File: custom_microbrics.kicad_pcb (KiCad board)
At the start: 2 copper layers, 20.2 x 20.2 mm, 2 parts, among them J1 Conn_01x03

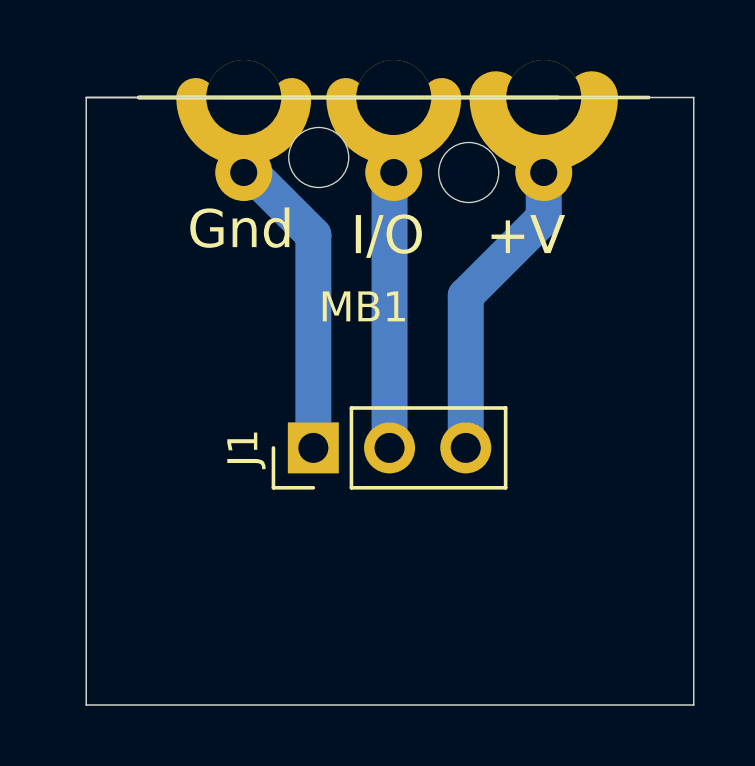
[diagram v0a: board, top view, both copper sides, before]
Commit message: schematic and pcb for psuedo breadboard
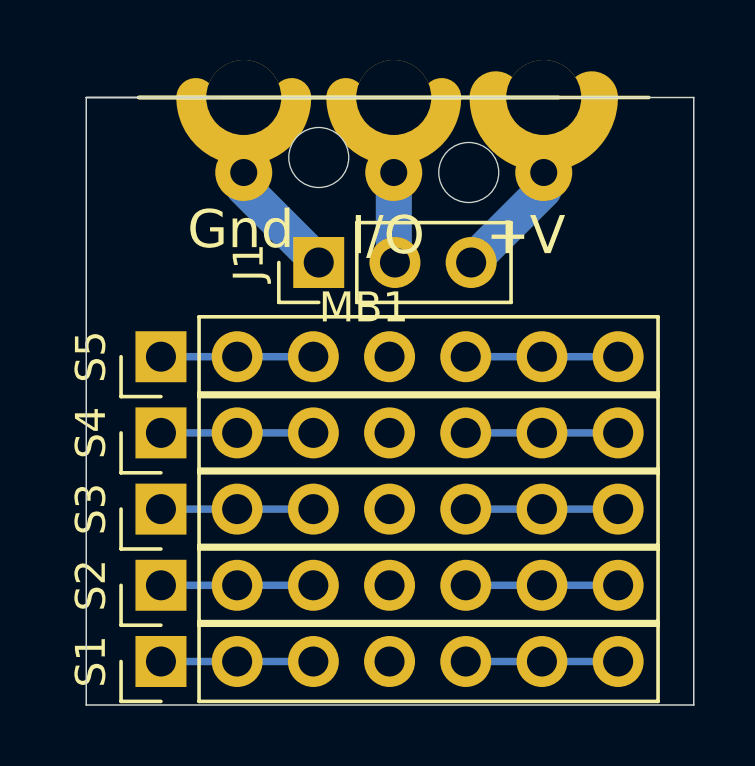
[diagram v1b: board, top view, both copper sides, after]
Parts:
- added S1: Conn_01x07, Connector_PinHeader_2.54mm:PinHeader_1x07_P2.54mm_Vertical, F.Cu at (142.2, 114.3)
- added S2: Conn_01x07, Connector_PinHeader_2.54mm:PinHeader_1x07_P2.54mm_Vertical, F.Cu at (142.2, 111.8)
- added S3: Conn_01x07, Connector_PinHeader_2.54mm:PinHeader_1x07_P2.54mm_Vertical, F.Cu at (142.2, 109.2)
- added S4: Conn_01x07, Connector_PinHeader_2.54mm:PinHeader_1x07_P2.54mm_Vertical, F.Cu at (142.2, 106.7)
- added S5: Conn_01x07, Connector_PinHeader_2.54mm:PinHeader_1x07_P2.54mm_Vertical, F.Cu at (142.2, 104.1)
- moved J1 6.18 mm to (147.5, 101.0)
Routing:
- net Net-(J1-Pad2): track 12.0 -> 3.02 mm
- net Net-(J1-Pad1): track 13.0 -> 4.04 mm
- net Net-(J1-Pad3): track 12.8 -> 6.50 mm
- net Net-(S5-Pad5): track 0.00 -> 5.08 mm
- net Net-(S5-Pad1): track 0.00 -> 5.08 mm
- net Net-(S4-Pad5): track 0.00 -> 5.08 mm
- net Net-(S4-Pad1): track 0.00 -> 5.08 mm
- net Net-(S3-Pad5): track 0.00 -> 5.08 mm
- net Net-(S3-Pad1): track 0.00 -> 5.08 mm
- net Net-(S2-Pad5): track 0.00 -> 5.08 mm
- net Net-(S2-Pad1): track 0.00 -> 5.08 mm
- net Net-(S1-Pad5): track 0.00 -> 5.08 mm
- net Net-(S1-Pad1): track 0.00 -> 5.08 mm

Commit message: minor tweaks
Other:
- rule trace_min: 0.2 -> 0.4

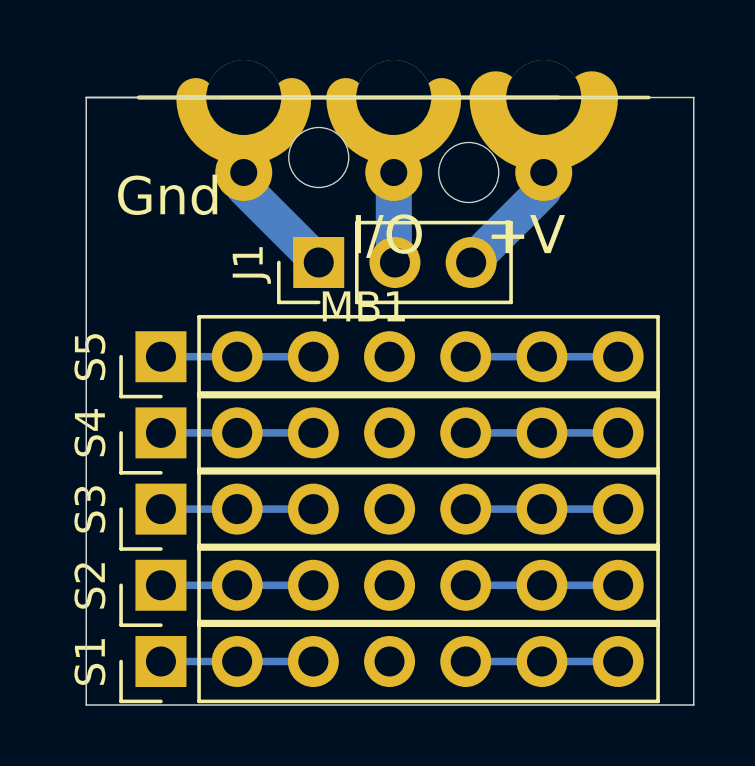
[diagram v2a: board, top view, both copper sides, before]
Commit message: initial design of stripboard2 layout, rotated rows/columns, and added optional smt LED (with jumper to configure between power or gpio-tied output)
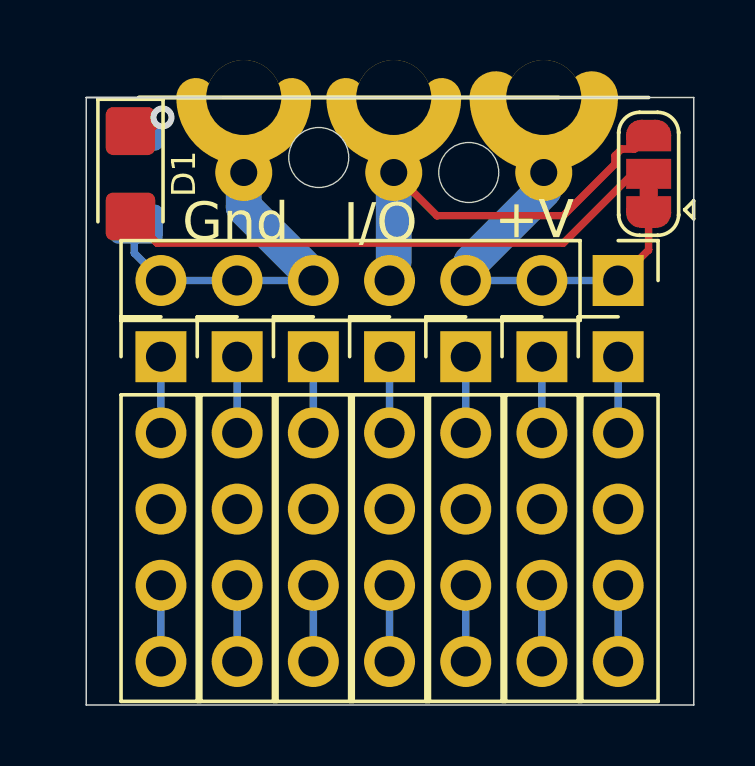
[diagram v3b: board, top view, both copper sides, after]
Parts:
- removed S1, S2, S3, S4, S5: Conn_01x07, Connector_PinHeader_2.54mm:PinHeader_1x07_P2.54mm_Vertical
- added D1: LED, LED_SMD:LED_1206_3216Metric_Castellated, F.Cu at (141.2, 98.0)
- added J2: Conn_01x05, Connector_PinHeader_2.54mm:PinHeader_1x05_P2.54mm_Vertical, F.Cu at (144.8, 104.1)
- added J3: Conn_01x05, Connector_PinHeader_2.54mm:PinHeader_1x05_P2.54mm_Vertical, F.Cu at (147.3, 104.1)
- added J4: Conn_01x05, Connector_PinHeader_2.54mm:PinHeader_1x05_P2.54mm_Vertical, F.Cu at (149.9, 104.1)
- added J5: Conn_01x05, Connector_PinHeader_2.54mm:PinHeader_1x05_P2.54mm_Vertical, F.Cu at (152.4, 104.1)
- added J6: Conn_01x07, Connector_PinHeader_2.54mm:PinHeader_1x07_P2.54mm_Vertical, F.Cu at (157.5, 101.6)
- added J7: Conn_01x05, Connector_PinHeader_2.54mm:PinHeader_1x05_P2.54mm_Vertical, F.Cu at (154.9, 104.1)
- added J8: Conn_01x05, Connector_PinHeader_2.54mm:PinHeader_1x05_P2.54mm_Vertical, F.Cu at (157.5, 104.1)
- added JP1: SolderJumper_3_Bridged12, Jumper:SolderJumper-3_P1.3mm_Bridged12_RoundedPad1.0x1.5mm, F.Cu at (158.5, 98.0)
- added R1: R_Small, Resistor_SMD:R_1206_3216Metric_Pad1.30x1.75mm_HandSolder, B.Cu at (141.4, 98.2)
- J1: value Conn_01x03 -> Conn_01x05; footprint Connector_PinHeader_2.54mm:PinHeader_1x03_P2.54mm_Vertical -> Connector_PinHeader_2.54mm:PinHeader_1x05_P2.54mm_Vertical
- moved J1 6.13 mm to (142.2, 104.1), turned to 0 degrees
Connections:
- J1 pad 2: Net-(J1-Pad2) -> Net-(J1-Pad1)
- J1 pad 3: Net-(J1-Pad3) -> (no net)
- MB1 pad 1: Net-(J1-Pad1) -> Net-(J6-Pad5)
- MB1 pad 2: Net-(J1-Pad2) -> Net-(J6-Pad4)
- MB1 pad 3: Net-(J1-Pad3) -> Net-(J6-Pad1)
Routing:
- net Net-(D1-Pad2): track 0.00 -> 18.6 mm
- net Net-(J6-Pad4): track 0.00 -> 15.7 mm
- net Net-(J6-Pad1): track 0.00 -> 14.3 mm
- net Net-(J6-Pad5): track 0.00 -> 14.0 mm
- net Net-(J1-Pad3): track 6.50 -> 0.00 mm
- net Net-(S5-Pad5): track 5.08 -> 0.00 mm
- net Net-(S5-Pad1): track 5.08 -> 0.00 mm
- net Net-(S4-Pad5): track 5.08 -> 0.00 mm
- net Net-(S4-Pad1): track 5.08 -> 0.00 mm
- net Net-(S3-Pad5): track 5.08 -> 0.00 mm
- net Net-(S3-Pad1): track 5.08 -> 0.00 mm
- net Net-(S2-Pad5): track 5.08 -> 0.00 mm
- net Net-(S2-Pad1): track 5.08 -> 0.00 mm
- net Net-(S1-Pad5): track 5.08 -> 0.00 mm
- net Net-(S1-Pad1): track 5.08 -> 0.00 mm
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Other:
- rule trace_min: 0.4 -> 0.1

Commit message: added silkscreen layer to match electrical connections
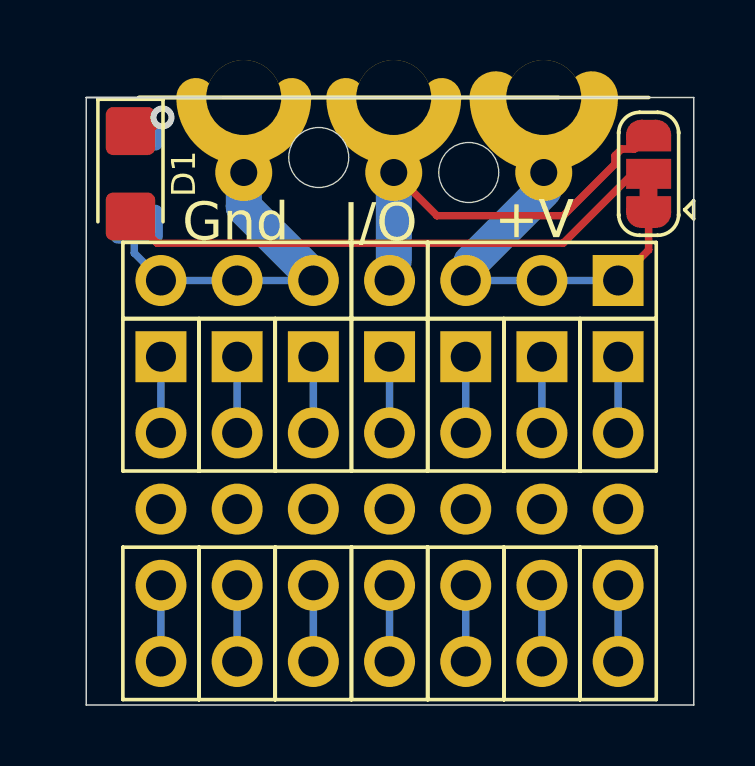
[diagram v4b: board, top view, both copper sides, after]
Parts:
- J1, J2, J3, J4, J5, J7, J8: footprint Connector_PinHeader_2.54mm:PinHeader_1x05_P2.54mm_Vertical -> custom-microbrics:PinHeader_1x05_P2.54mm_Vertical_BreadBoardySilkScreen
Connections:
- J1 pad 3: (no net) -> Net-(J1-Pad3)
- J2 pad 3: (no net) -> Net-(J2-Pad3)
- J3 pad 3: (no net) -> Net-(J3-Pad3)
- J4 pad 3: (no net) -> Net-(J4-Pad3)
- J5 pad 3: (no net) -> Net-(J5-Pad3)
- J7 pad 3: (no net) -> Net-(J7-Pad3)
- J8 pad 3: (no net) -> Net-(J8-Pad3)

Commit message: switch unneeded silkscreen to dwgs.user
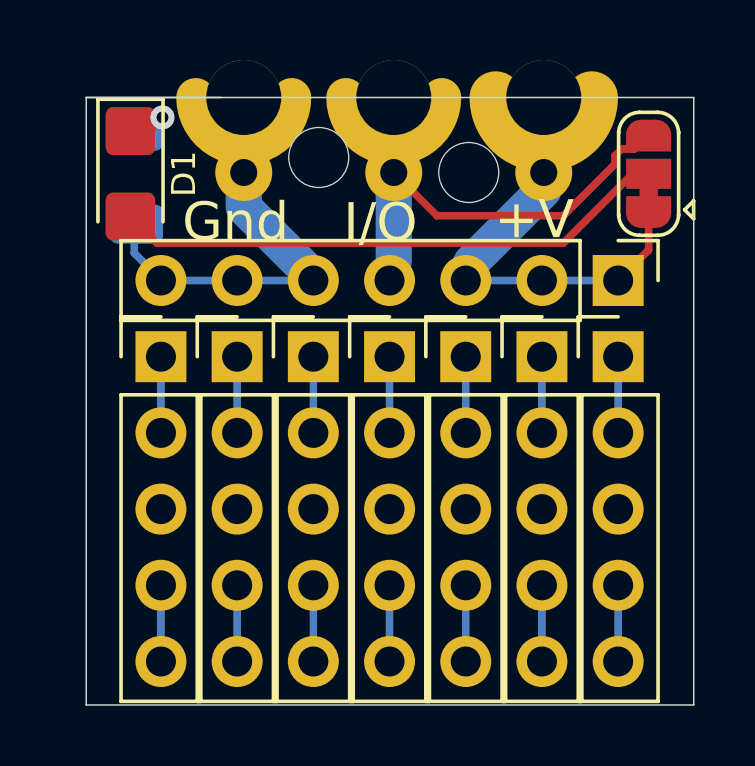
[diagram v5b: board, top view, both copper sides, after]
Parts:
- J1, J2, J3, J4, J5, J7, J8: footprint custom-microbrics:PinHeader_1x05_P2.54mm_Vertical_BreadBoardySilkScreen -> Connector_PinHeader_2.54mm:PinHeader_1x05_P2.54mm_Vertical
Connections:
- J1 pad 3: Net-(J1-Pad3) -> (no net)
- J2 pad 3: Net-(J2-Pad3) -> (no net)
- J3 pad 3: Net-(J3-Pad3) -> (no net)
- J4 pad 3: Net-(J4-Pad3) -> (no net)
- J5 pad 3: Net-(J5-Pad3) -> (no net)
- J7 pad 3: Net-(J7-Pad3) -> (no net)
- J8 pad 3: Net-(J8-Pad3) -> (no net)

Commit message: fix accidentally overwritten file in previous commit
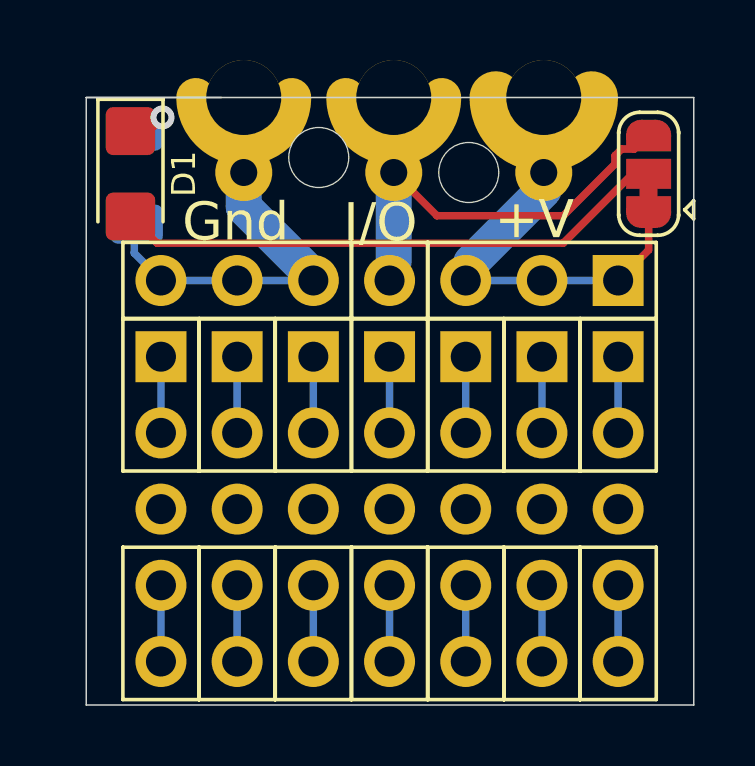
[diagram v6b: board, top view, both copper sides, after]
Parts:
- J1, J2, J3, J4, J5, J7, J8: footprint Connector_PinHeader_2.54mm:PinHeader_1x05_P2.54mm_Vertical -> custom-microbrics:PinHeader_1x05_P2.54mm_Vertical_BreadBoardySilkScreen
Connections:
- J1 pad 3: (no net) -> Net-(J1-Pad3)
- J2 pad 3: (no net) -> Net-(J2-Pad3)
- J3 pad 3: (no net) -> Net-(J3-Pad3)
- J4 pad 3: (no net) -> Net-(J4-Pad3)
- J5 pad 3: (no net) -> Net-(J5-Pad3)
- J7 pad 3: (no net) -> Net-(J7-Pad3)
- J8 pad 3: (no net) -> Net-(J8-Pad3)
